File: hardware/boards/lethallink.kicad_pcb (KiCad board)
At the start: 6 copper layers, 86 x 111.1 mm, 146 parts, among them J1 PCIe-x4, J2 USB3_Micro_B_Amphenol, J3 Conn_02x05_Odd_Even, Q1 Q_NMOS_GSD, Q2 Q_NMOS_GSD, Q3 Q_NMOS_GSD, Q4 Q_NMOS_GSD, Q5 SI7232DN-T1-GE3, SW1 SW_DIP_x03, U1 ECP5UM5G-381caBGA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

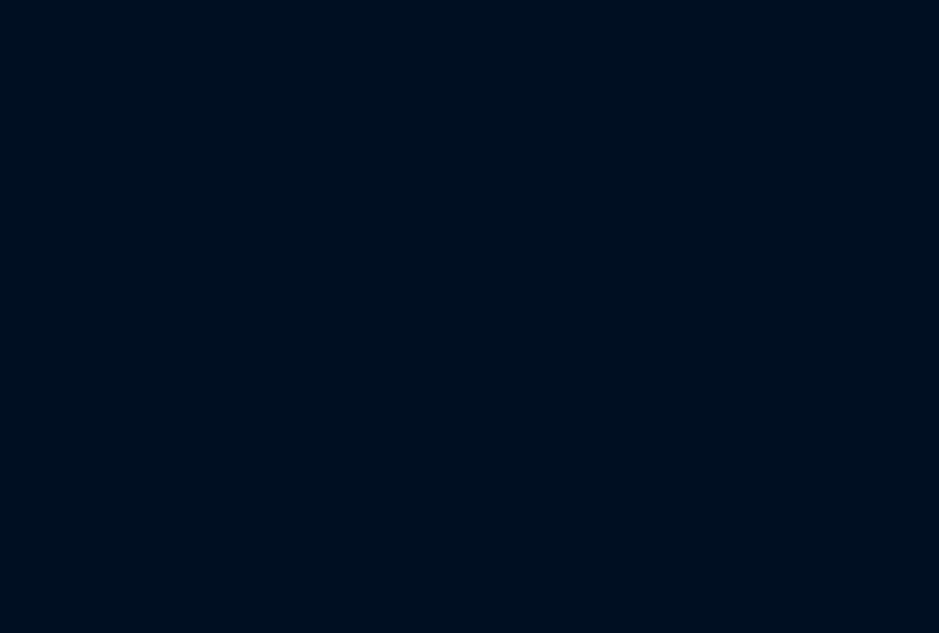
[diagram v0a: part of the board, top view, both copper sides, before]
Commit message: Annotated the schematics and updated the PCB with the new imported parts
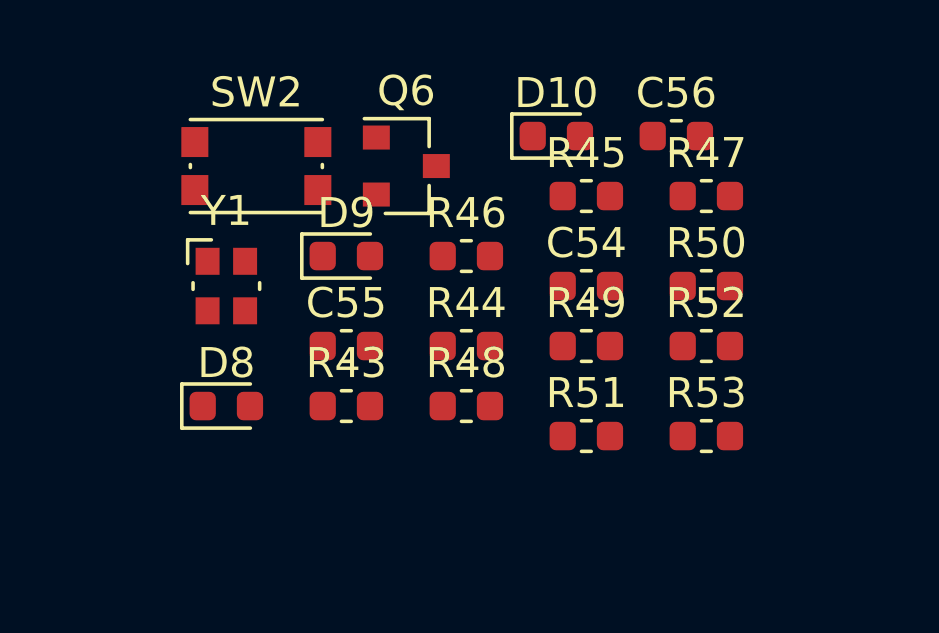
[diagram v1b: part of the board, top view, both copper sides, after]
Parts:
- added C54: 0.1uF, Capacitor_SMD:C_0603_1608Metric, F.Cu at (99.0, -50.0)
- added C55: 15pF, Capacitor_SMD:C_0603_1608Metric, F.Cu at (91.0, -48.0)
- added C56: 15pF, Capacitor_SMD:C_0603_1608Metric, F.Cu at (102.0, -55.0)
- added D10: PNK, LED_SMD:LED_0603_1608Metric, F.Cu at (98.0, -55.0)
- added D8: BLU, LED_SMD:LED_0603_1608Metric, F.Cu at (87.0, -46.0)
- added D9: RED, LED_SMD:LED_0603_1608Metric, F.Cu at (91.0, -51.0)
- added Q6: Q_NMOS_GSD, Package_TO_SOT_SMD:SOT-23, F.Cu at (93.0, -54.0)
- added R43: 10k, Resistor_SMD:R_0603_1608Metric, F.Cu at (91.0, -46.0)
- added R44: 10k, Resistor_SMD:R_0603_1608Metric, F.Cu at (95.0, -48.0)
- added R45: 10k, Resistor_SMD:R_0603_1608Metric, F.Cu at (99.0, -53.0)
- added R46: 10k, Resistor_SMD:R_0603_1608Metric, F.Cu at (95.0, -51.0)
- added R47: 4k7, Resistor_SMD:R_0603_1608Metric, F.Cu at (103.0, -53.0)
- added R48: 10k, Resistor_SMD:R_0603_1608Metric, F.Cu at (95.0, -46.0)
- added R49: 10k, Resistor_SMD:R_0603_1608Metric, F.Cu at (99.0, -48.0)
- added R50: 10k, Resistor_SMD:R_0603_1608Metric, F.Cu at (103.0, -50.0)
- added R51: 10k, Resistor_SMD:R_0603_1608Metric, F.Cu at (99.0, -45.0)
- added R52: 6k04, Resistor_SMD:R_0603_1608Metric, F.Cu at (103.0, -48.0)
- added R53: 200, Resistor_SMD:R_0603_1608Metric, F.Cu at (103.0, -45.0)
- added SW2: RESET, Button_Switch_SMD:SW_Push_1P1T_NO_CK_KMR2, F.Cu at (88.0, -54.0)
- added Y1: 19.2MHz, Crystal:Crystal_SMD_Abracon_ABM10-4Pin_2.5x2.0mm, F.Cu at (87.0, -50.0)
- R42: value 1k -> 50
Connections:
- FB10 pad 1: /IC Power/VBUS -> /USB3 Interface/VBUS
- FB10 pad 2: /USB3 Interface/VBUS -> /IC Power/VBUS
- J3 pad 1: Net-(J3-Pad1) -> +3V3
- J3 pad 10: Net-(J3-Pad10) -> Net-(C54-Pad2)
- U1 pad U3: Net-(R42-Pad1) -> Net-(R42-Pad2)
- U1 pad V2: Net-(U1-PadV2) -> Net-(R46-Pad2)
- U1 pad W1: Net-(U1-PadW1) -> Net-(R45-Pad2)
- U1 pad W2: Net-(U1-PadW2) -> Net-(R44-Pad2)
- U1 pad W3: Net-(U1-PadW3) -> Net-(C54-Pad2)
- U1 pad Y2: Net-(U1-PadY2) -> Net-(R43-Pad2)
- U3 pad B11: Net-(U3-PadB11) -> Net-(C54-Pad2)
- U5 pad 1: Net-(U5-Pad1) -> Net-(U1-PadR2)
- U5 pad 2: Net-(U5-Pad2) -> Net-(R44-Pad2)
- U5 pad 3: Net-(U5-Pad3) -> Net-(R43-Pad2)
- U5 pad 5: Net-(U5-Pad5) -> Net-(R46-Pad2)
- U5 pad 6: Net-(R42-Pad2) -> Net-(R42-Pad1)
- U5 pad 7: Net-(U5-Pad7) -> Net-(R45-Pad2)
- U6 pad 1: Net-(U6-Pad1) -> Net-(U3-PadC1)
- U6 pad 2: Net-(U6-Pad2) -> Net-(U3-PadC2)
- U6 pad 5: Net-(U6-Pad5) -> Net-(U3-PadD5)
- U6 pad 6: Net-(U6-Pad6) -> Net-(U3-PadD4)

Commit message: Added the 3D model to the crystal
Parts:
- Y1: footprint Crystal:Crystal_SMD_Abracon_ABM10-4Pin_2.5x2.0mm -> lethalbit:Crystal_SMD_Abracon_ABM10-4Pin_2.5x2.0mm
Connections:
- U3 pad B2: Net-(U3-PadB2) -> GND
- U3 pad B4: Net-(U3-PadB4) -> GND
- U3 pad E6: Net-(U3-PadE6) -> GND

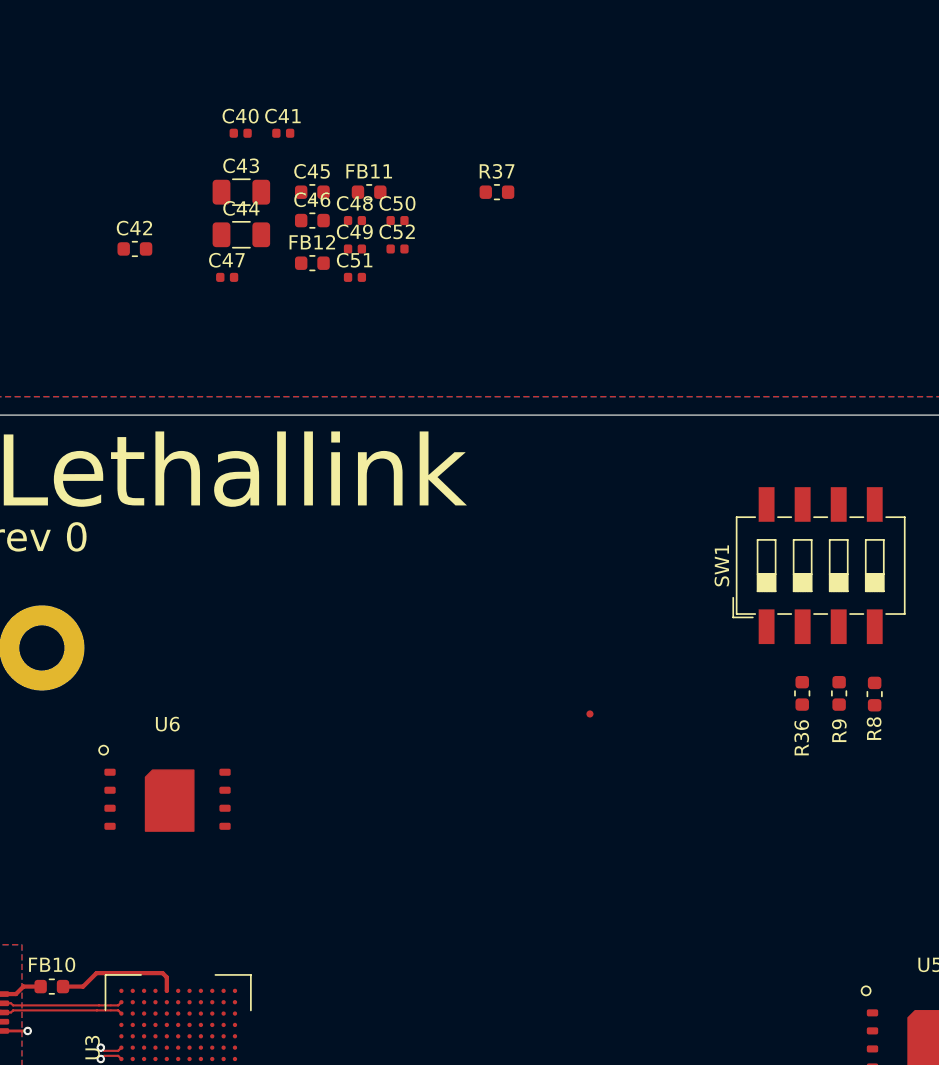
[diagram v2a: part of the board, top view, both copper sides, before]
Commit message: Updated the PCB with the new parts for PHY reset logic and added another fiducial for the other SPI flash
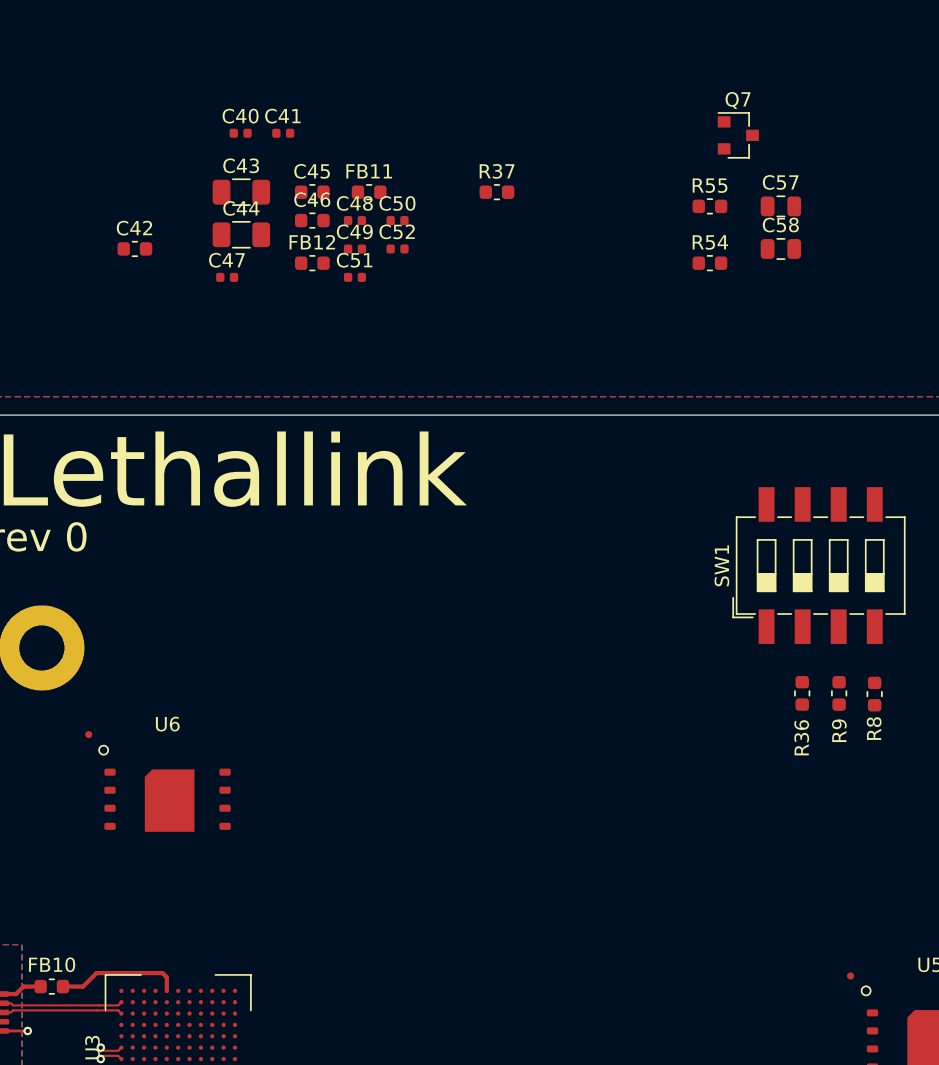
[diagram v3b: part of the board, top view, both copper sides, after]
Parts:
- added C57: 22uF, Capacitor_SMD:C_0805_2012Metric, F.Cu at (77.0, 1.00)
- added C58: 22uF, Capacitor_SMD:C_0805_2012Metric, F.Cu at (77.0, 4.00)
- added FID6: Fiducial, Fiducial:Fiducial_0.5mm_Mask1mm, F.Cu at (81.9, 55.2)
- added Q7: Q_NMOS_GSD, Package_TO_SOT_SMD:SOT-23, F.Cu at (74.0, -4.00)
- added R54: 10k, Resistor_SMD:R_0603_1608Metric, F.Cu at (72.0, 5.00)
- added R55: 1k, Resistor_SMD:R_0603_1608Metric, F.Cu at (72.0, 1.00)
- moved FID4 35.3 mm to (28.2, 38.2)
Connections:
- net Net-(U3-PadL8) renamed /Boot Config/~PHY_INT
- U3 pad A2: Net-(U3-PadA2) -> +1V2
- U3 pad A7: Net-(U3-PadA7) -> +1V2
- U3 pad B1: Net-(U3-PadB1) -> +1V8
- U3 pad B5: Net-(U3-PadB5) -> +1V2
- U3 pad B6: Net-(U3-PadB6) -> +1V8
- U3 pad C11: Net-(U3-PadC11) -> +3V3
- U3 pad E10: Net-(U3-PadE10) -> /IC Power/VBUS
- U3 pad E3: Net-(U3-PadE3) -> +1V8
- U3 pad F1: Net-(U3-PadF1) -> +1V8
- U3 pad H11: Net-(U3-PadH11) -> +1V8
- U3 pad L9: Net-(U3-PadL9) -> +1V8

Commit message: Added headers for the SPI flash for both the FPGA and the PHY
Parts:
- added J4: Conn_02x04_Odd_Even, Connector_PinHeader_1.27mm:PinHeader_2x05_P1.27mm_Vertical, F.Cu at (90.0, 49.8)
- added J5: Conn_02x04_Odd_Even, Connector_PinHeader_1.27mm:PinHeader_2x05_P1.27mm_Vertical, F.Cu at (36.2, 33.2)
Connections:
- net Net-(R54-Pad1) renamed /Boot Config/~PHY_RESET

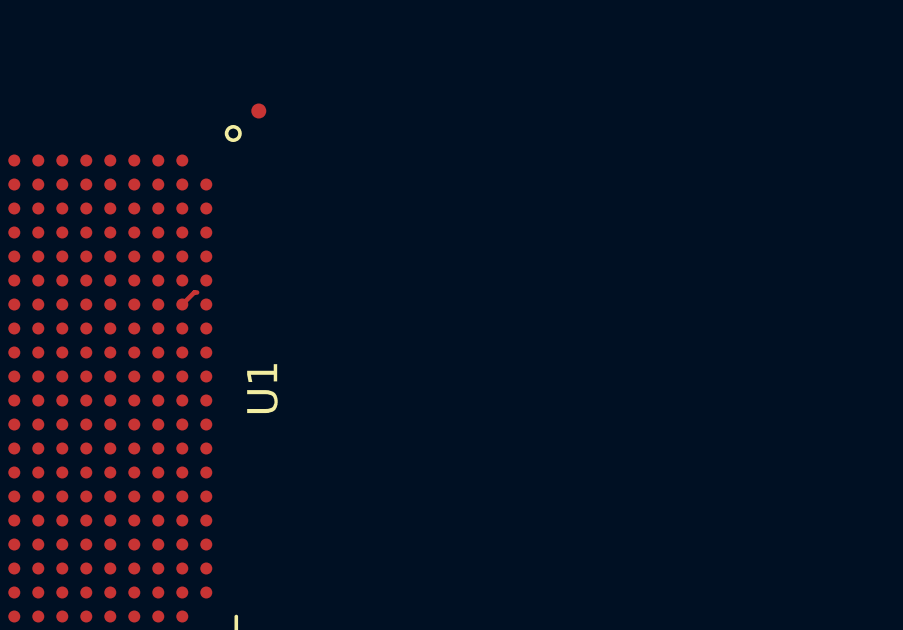
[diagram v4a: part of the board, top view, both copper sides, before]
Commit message: Added the main OSC for the FPGA
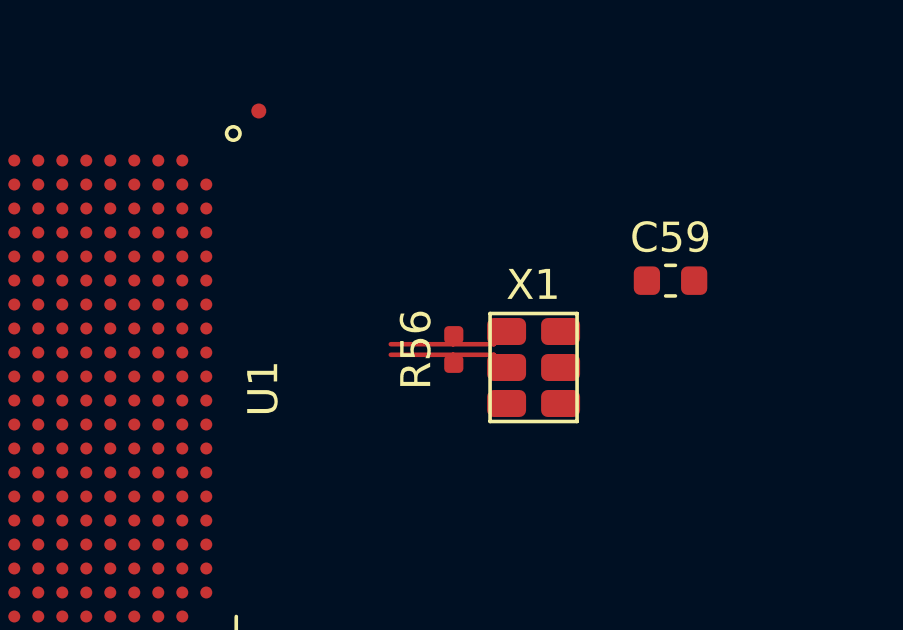
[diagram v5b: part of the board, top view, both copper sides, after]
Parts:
- added C59: 0.1uF, Capacitor_SMD:C_0603_1608Metric, F.Cu at (110.0, 86.3)
- added R56: 100, Resistor_SMD:R_0402_1005Metric, F.Cu at (102.8, 88.5)
- added X1: AX3, lethalbit:AX3, F.Cu at (105.4, 89.2)
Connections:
- U1 pad B11: Net-(U1-PadB11) -> /AUX Control/CLK+
- U1 pad C11: Net-(U1-PadC11) -> /AUX Control/CLK-
- U3 pad B1: +1V8 -> +3V3
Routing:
- net /AUX Control/CLK-: track 0.00 -> 4.36 mm
- net /AUX Control/CLK+: track 0.00 -> 4.36 mm
- net GND: track 60.2 -> 59.5 mm

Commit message: Hooked up most of the GPIF II bus to the the FPGA
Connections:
- U1 pad N19: Net-(U1-PadN19) -> /USB3 Interface/GPIF_00
- U1 pad N20: Net-(U1-PadN20) -> /USB3 Interface/GPIF_01
- U1 pad P18: Net-(U1-PadP18) -> /USB3 Interface/GPIF_03
- U1 pad P19: Net-(U1-PadP19) -> /USB3 Interface/GPIF_02
- U1 pad P20: Net-(U1-PadP20) -> /USB3 Interface/GPIF_04
- U1 pad R18: Net-(U1-PadR18) -> /USB3 Interface/GPIF_09
- U1 pad R20: Net-(U1-PadR20) -> /USB3 Interface/GPIF_05
- U1 pad T17: Net-(U1-PadT17) -> /USB3 Interface/GPIF_15
- U1 pad T18: Net-(U1-PadT18) -> /USB3 Interface/GPIF_11
- U1 pad T19: Net-(U1-PadT19) -> /USB3 Interface/GPIF_08
- U1 pad T20: Net-(U1-PadT20) -> /USB3 Interface/GPIF_06
- U1 pad U16: Net-(U1-PadU16) -> /USB3 Interface/GPIF_14
- U1 pad U17: Net-(U1-PadU17) -> /USB3 Interface/GPIF_13
- U1 pad U18: Net-(U1-PadU18) -> /USB3 Interface/GPIF_12
- U1 pad U19: Net-(U1-PadU19) -> /USB3 Interface/GPIF_10
- U1 pad U20: Net-(U1-PadU20) -> /USB3 Interface/GPIF_07
- U3 pad D1: Net-(U3-PadD1) -> /USB3 Interface/GPIF_13
- U3 pad D2: Net-(U3-PadD2) -> /USB3 Interface/GPIF_14
- U3 pad D3: Net-(U3-PadD3) -> /USB3 Interface/GPIF_15
- U3 pad E1: Net-(U3-PadE1) -> /USB3 Interface/GPIF_10
- U3 pad E4: Net-(U3-PadE4) -> /USB3 Interface/GPIF_12
- U3 pad E5: Net-(U3-PadE5) -> /USB3 Interface/GPIF_11
- U3 pad F2: Net-(U3-PadF2) -> /USB3 Interface/GPIF_08
- U3 pad F3: Net-(U3-PadF3) -> /USB3 Interface/GPIF_07
- U3 pad F4: Net-(U3-PadF4) -> /USB3 Interface/GPIF_04
- U3 pad F5: Net-(U3-PadF5) -> /USB3 Interface/GPIF_09
- U3 pad G2: Net-(U3-PadG2) -> /USB3 Interface/GPIF_05
- U3 pad G3: Net-(U3-PadG3) -> /USB3 Interface/GPIF_06
- U3 pad H2: Net-(U3-PadH2) -> /USB3 Interface/GPIF_02
- U3 pad H3: Net-(U3-PadH3) -> /USB3 Interface/GPIF_03
- U3 pad J1: Net-(U3-PadJ1) -> /USB3 Interface/GPIF_01
- U3 pad J3: Net-(U3-PadJ3) -> /USB3 Interface/GPIF_00
